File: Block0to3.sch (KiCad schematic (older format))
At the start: 144 parts, among them J1 PA, J10 PK, J11 PM, J12 PO, J13 PJ, J14 PL, J15 PN, J16 PP, J17 PQ, J18 PS, J19 PU, J2 PC, J20 PW, J21 PR, J22 PT, J23 PV, J24 PX, J25 PY, J26 PAA, J27 PAC, J28 PAE, J29 PZ, J3 PE, J30 PAB, J31 PAD, J32 PAF, J4 PG, J5 PB, J6 PD, J7 PF, J8 PH, J9 PI, U1 AW9523B, U10 AW9523B, U11 AW9523B, U12 AW9523B, U13 AW9523B, U14 AW9523B, U15 AW9523B, U16 AW9523B, U2 AW9523B, U3 AW9523B, U4 AW9523B, U5 AW9523B, U6 AW9523B, U7 AW9523B, U8 AW9523B, U9 AW9523B

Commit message: Continue Routing
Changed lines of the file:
@@
 Wire Bus Line
 	11350 1650 7550 1650
+Text Label 3550 1550 2    50   ~ 0
+SCL[0..7]
+Text Label 3550 1650 2    50   ~ 0
+SDA[0..7]
 $EndSCHEMATC

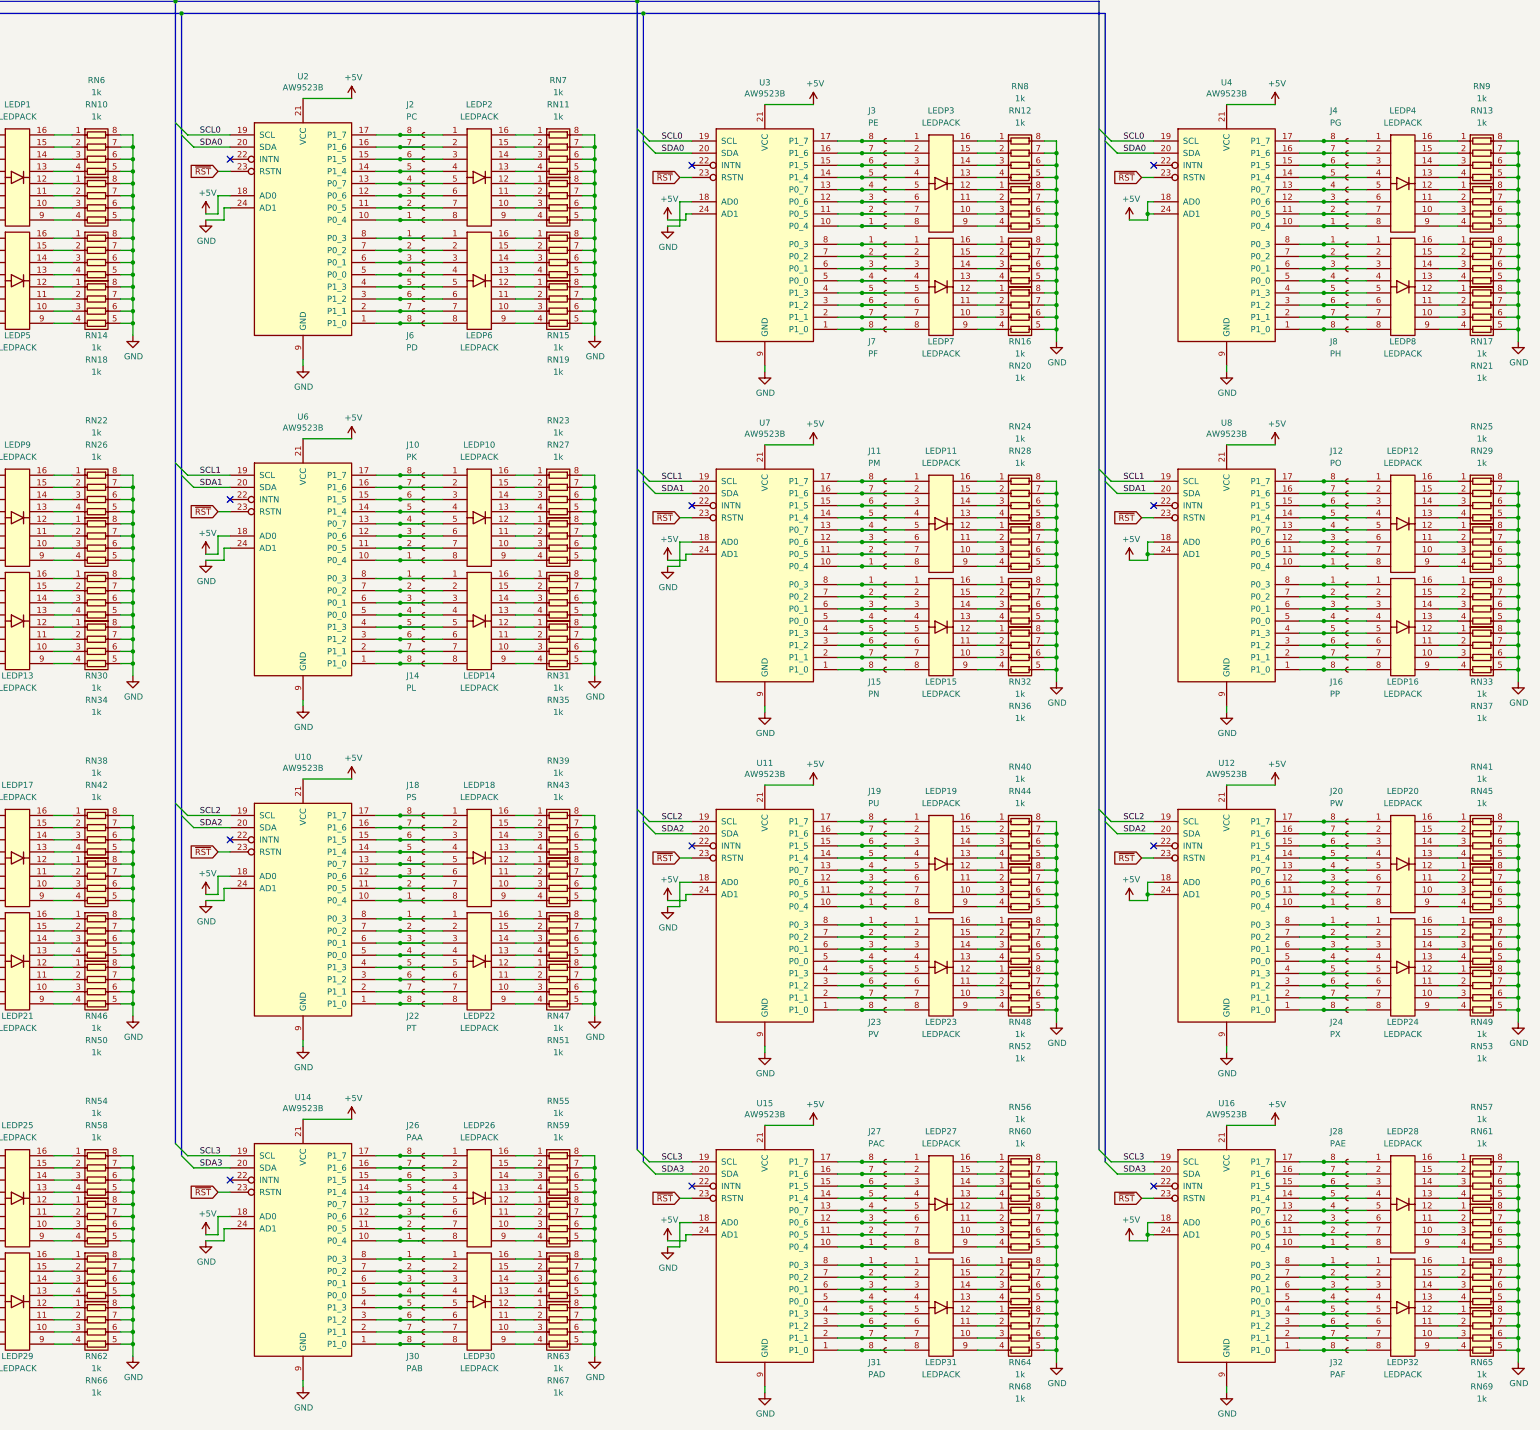
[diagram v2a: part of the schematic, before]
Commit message: Change some C and R values
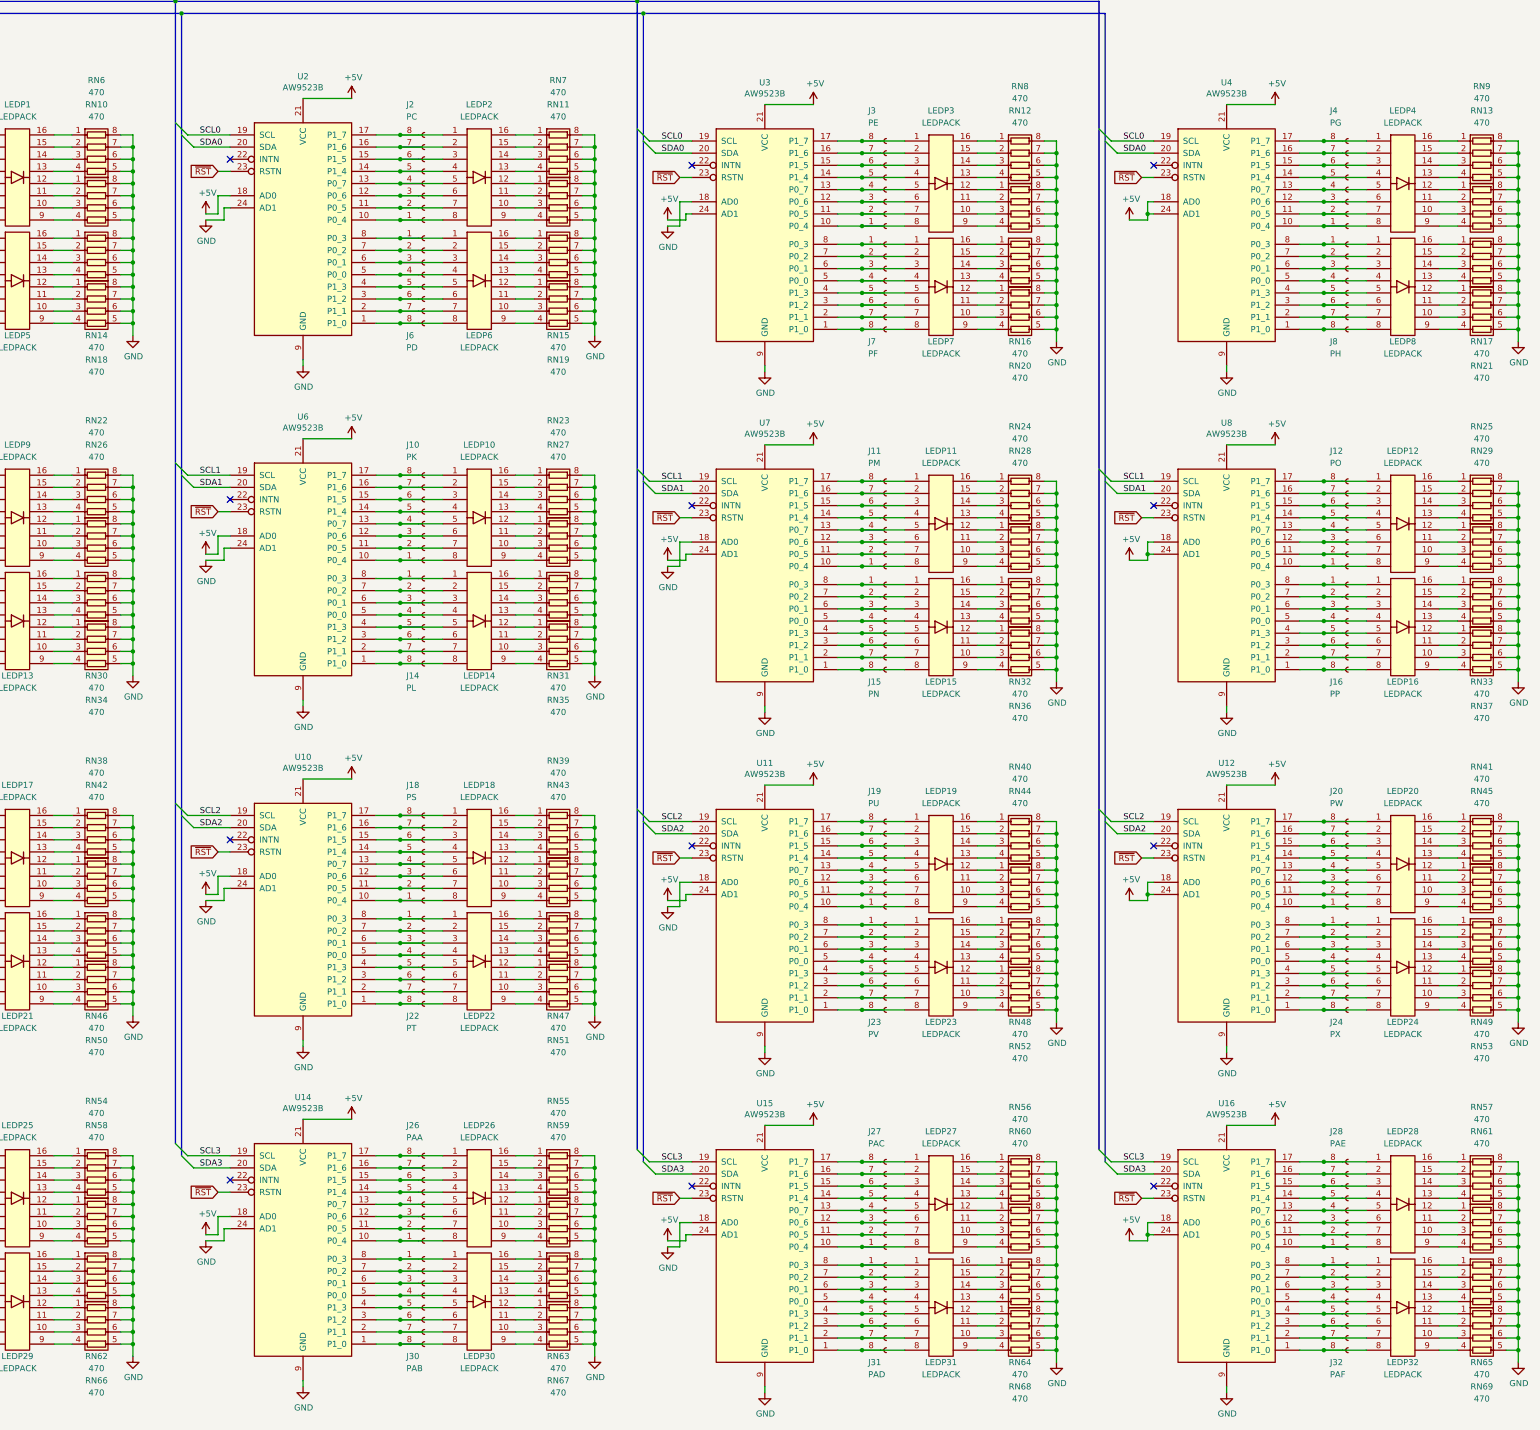
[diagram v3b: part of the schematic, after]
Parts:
- RN10, RN11, RN12, RN13, RN14, RN15, RN16, RN17, RN18, RN19, RN20, RN21, RN22, RN23, RN24, RN25, RN26, RN27, RN28, RN29, RN30, RN31, RN32, RN33, RN34, RN35, RN36, RN37, RN38, RN39, RN40, RN41, RN42, RN43, RN44, RN45, RN46, RN47, RN48, RN49, RN50, RN51, RN52, RN53, RN54, RN55, RN56, RN57, RN58, RN59, RN6, RN60, RN61, RN62, RN63, RN64, RN65, RN66, RN67, RN68, RN69, RN7, RN8, RN9: value 1k -> 470
